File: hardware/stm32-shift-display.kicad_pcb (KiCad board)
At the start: 2 copper layers, 93.5 x 48.3 mm, 117 parts, among them J1 HDR_SWD, J2 USB_C_Receptacle_USB2.0_16P, SW1 SW_PUSH, SW2 SW_PUSH, SW3 SW_PUSH, SW4 SW_PUSH, SW5 218-2LPSTR, U1 AMS1117-3.3, U10 74HC595, U11 74HC595, U12 SM420561N, U13 SM420561N, U14 SM420561N, U2 STM32F103C8T6, U3 74HC595, U4 74HC595, U5 74HC595, U6 SM420561N, U7 SM420561N, U8 SM420561N, U9 74HC595, X1 OT32258MJBA4SL, X2 OK322532.768KJBA4SL

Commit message: Pre-autoroute on rev2
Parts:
- removed D4: BAT43, Diode_THT:D_DO-35_SOD27_P7.62mm_Horizontal
- removed G***: LOGO, CustomSymbols:GrackleLogo12mm
- removed JP1: SolderJumper_2_Open, Jumper:SolderJumper-2_P1.3mm_Open_RoundedPad1.0x1.5mm
- removed R10, R9: 10R, Resistor_SMD:R_0402_1005Metric
- removed R11: 10k, Resistor_SMD:R_0402_1005Metric
- removed R14, R15, R16, R17, R18, R19, R20, R21, R22, R23, R24, R25, R26, R27, R28, R29, R30, R31, R32, R33, R34, R35, R36, R37, R38, R39, R40, R41, R42, R43, R44, R45, R46, R47, R48, R49, R50, R51, R52, R53, R54, R55, R56, R57, R58, R59, R60: 470R, Resistor_SMD:R_0603_1608Metric
- removed R61: 22R, Resistor_THT:R_Axial_DIN0207_L6.3mm_D2.5mm_P7.62mm_Horizontal
- removed X2: OK322532.768KJBA4SL, Crystal:Crystal_SMD_3225-4Pin_3.2x2.5mm
- added BT1: 1060TR, Battery:BatteryHolder_Keystone_1060_1x2032, F.Cu at (144.8, 91.4)
- added C19: 100n, Capacitor_SMD:C_0402_1005Metric, B.Cu at (164.5, 78.5)
- added J3: HDR_UART, Connector_PinHeader_2.54mm:PinHeader_1x05_P2.54mm_Vertical, F.Cu at (194.7, 91.3)
- added RN1: 220R, Resistor_SMD:R_Array_Convex_4x0603, B.Cu at (139.7, 71.1)
- added RN10: 220R, Resistor_SMD:R_Array_Convex_4x0603, B.Cu at (190.4, 71.1)
- added RN11: 220R, Resistor_SMD:R_Array_Convex_4x0603, B.Cu at (180.2, 66.8)
- added RN12: 220R, Resistor_SMD:R_Array_Convex_4x0603, B.Cu at (190.4, 66.8)
- added RN13: 220R, Resistor_SMD:R_Array_Convex_4x0603, B.Cu at (126.6, 75.2)
- added RN2: 220R, Resistor_SMD:R_Array_Convex_4x0603, B.Cu at (149.7, 71.1)
- added RN3: 220R, Resistor_SMD:R_Array_Convex_4x0603, B.Cu at (139.7, 66.5)
- added RN4: 220R, Resistor_SMD:R_Array_Convex_4x0603, B.Cu at (149.7, 66.8)
- added RN5: 220R, Resistor_SMD:R_Array_Convex_4x0603, B.Cu at (159.9, 71.1)
- added RN6: 220R, Resistor_SMD:R_Array_Convex_4x0603, B.Cu at (170.1, 71.1)
- added RN7: 220R, Resistor_SMD:R_Array_Convex_4x0603, B.Cu at (159.9, 66.8)
- added RN8: 220R, Resistor_SMD:R_Array_Convex_4x0603, B.Cu at (170.1, 66.8)
- added RN9: 220R, Resistor_SMD:R_Array_Convex_4x0603, B.Cu at (180.2, 71.1)
- added U15: 74HC595, Package_SO:SOIC-16_3.9x9.9mm_P1.27mm, B.Cu at (166.9, 84.3)
- added Y1: Q13FC13500002, Crystal:Crystal_SMD_3215-2Pin_3.2x1.5mm, B.Cu at (174.1, 86.3)
- C1, C14, C15, C16, C17, C2, C6, C7, C8, R1, R12, SW5, U10, U11, U2, X1: moved to B.Cu
- C10, C9: value 100n -> 6p; moved to B.Cu
- C11, C12: footprint Capacitor_SMD:C_0402_1005Metric -> Capacitor_SMD:C_0805_2012Metric; moved to B.Cu
- C13: value 100n -> 10u; footprint Capacitor_SMD:C_0402_1005Metric -> Capacitor_Tantalum_SMD:CP_EIA-3216-18_Kemet-A; moved to B.Cu
- C18: value SCMR22C155PRBA0 -> 100n; footprint Mouser:SCMR22C155PRBA0 -> Capacitor_SMD:C_0402_1005Metric; moved to B.Cu
- C3, C4: footprint Capacitor_SMD:C_0805_2012Metric -> Capacitor_SMD:C_0402_1005Metric; moved to B.Cu
- C5: value 10u -> 100n; footprint Capacitor_Tantalum_SMD:CP_EIA-3216-18_Kemet-A -> Capacitor_SMD:C_0402_1005Metric; moved to B.Cu
- D1, D2, D3: value KT-0805Y -> LED_YLW; footprint LED_SMD:LED_0805_2012Metric -> LED_THT:LED_D3.0mm
- H1, H2, H3, H4: footprint MountingHole:MountingHole_3.2mm_M3_Pad_Via -> MountingHole:MountingHole_3.2mm_M3_ISO7380
- J1: value HDR_SWD -> GT-USB-7010ASV; footprint Connector_PinHeader_2.54mm:PinHeader_1x04_P2.54mm_Vertical -> easyeda2kicad:USB-C-SMD_G-SWITCH_GT-USB-7010ASV; moved to B.Cu
- J2: value USB_C_Receptacle_USB2.0_16P -> HDR_SWD; footprint Connector_USB:USB_C_Receptacle_HCTL_HC-TYPE-C-16P-01A -> Connector_PinHeader_2.54mm:PinHeader_1x04_P2.54mm_Vertical
- R13: value 470R -> 10k; footprint Resistor_SMD:R_0603_1608Metric -> Resistor_SMD:R_0402_1005Metric; moved to B.Cu
- R2, R3: value 10k -> 5k1; moved to B.Cu
- R4, R5: value 220R -> 0R; footprint Resistor_SMD:R_0603_1608Metric -> Resistor_SMD:R_0402_1005Metric; moved to B.Cu
- R6: value 220R -> 1k5; footprint Resistor_SMD:R_0603_1608Metric -> Resistor_SMD:R_0402_1005Metric; moved to B.Cu
- R7, R8: value 5k1 -> 10k; moved to B.Cu
- SW1: value SW_PUSH -> TS-1101-C-W; footprint Button_Switch_THT:SW_PUSH_6mm -> easyeda2kicad:SW-SMD_L6.0-W3.3-LS8.0; moved to B.Cu
- SW2, SW3, SW4: footprint Button_Switch_THT:SW_PUSH_6mm -> Mouser:TS046643BK160SMT
- U1: value AMS1117-3.3 -> USBLC6-2P6; footprint Package_TO_SOT_SMD:SOT-223-3_TabPin2 -> Package_TO_SOT_SMD:SOT-666; moved to B.Cu
- U12, U13, U8: value SM420561N -> VDMY10C0; footprint Display_7Segment:7SegmentLED_LTS6760_LTS6780 -> Mouser:VDMx10x0
- U14, U6, U7: value SM420561N -> 74HC595; footprint Display_7Segment:7SegmentLED_LTS6760_LTS6780 -> Package_SO:SOIC-16_3.9x9.9mm_P1.27mm; moved to B.Cu
- U3: value 74HC595 -> AMS1117-3.3; footprint Package_SO:SOIC-16_3.9x9.9mm_P1.27mm -> Package_TO_SOT_SMD:SOT-223-3_TabPin2; moved to B.Cu
- U4, U5, U9: value 74HC595 -> VDMY10C0; footprint Package_SO:SOIC-16_3.9x9.9mm_P1.27mm -> Mouser:VDMx10x0
- moved H4 82.3 mm to (203.2, 99.1)
- moved H3 79.8 mm to (127.0, 99.1)
- moved R6 70.6 mm to (191.3, 86.4), turned to 90 degrees
- moved R5 69.9 mm to (190.8, 84.8)
- moved R4 69.9 mm to (190.8, 83.8)
- moved U3 69.1 mm to (200.2, 70.9)
- moved R12 68.1 mm to (138.0, 93.1), turned to -90 degrees
- moved TP1 62.8 mm to (177.3, 55.9), turned to 90 degrees
- moved C12 62.2 mm to (199.1, 65.3), turned to 180 degrees
- moved TP2 61.8 mm to (180.9, 55.9), turned to 90 degrees
- moved TP3 60.9 mm to (184.4, 55.9), turned to 90 degrees
- moved TP4 59.9 mm to (188.0, 55.9), turned to 90 degrees
- moved TP5 59.1 mm to (191.5, 55.9), turned to 90 degrees
- moved C17 52.8 mm to (148.7, 78.5), turned to 180 degrees
- moved C13 49.1 mm to (198.9, 76.7), turned to 180 degrees
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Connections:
- C1 pad 1: VCC -> VBAT
- C10 pad 1: VCC -> GND
- C10 pad 2: GND -> /OSC32_OUT
- C11 pad 1: VCC -> VBUS
- C18 pad 1: Net-(C18-Pad1) -> VCC
- C2 pad 1: VBAT -> VCC
- C3 pad 1: VBUS -> VCC
- C7 pad 1: VBAT -> VCC
- C8 pad 1: VCC -> VBUS
- C9 pad 1: VCC -> GND
- C9 pad 2: GND -> /OSC32_IN
- J1 pad 1: VCC -> GND
- J1 pad 2: /SWDIO -> GND
- J1 pad 3: /SWCLK -> GND
- R12 pad 2: /Shift Display/~{SRCLR} -> /Shift Display/~{OE}
- R13 pad 1: /Shift Display/Q1A -> VCC
- R13 pad 2: /Shift Display/D1B -> /Shift Display/~{SRCLR}
- R2 pad 2: /BOOT0 -> /CC1
- R3 pad 2: /BOOT1 -> /CC2
- R4 pad 1: /LED1r -> /MCU_D-
- R4 pad 2: /LED1 -> /ESD_D-
- R5 pad 1: /LED2r -> /MCU_D+
- R5 pad 2: /LED2 -> /ESD_D+
- R6 pad 1: /LED3r -> VCC
- R6 pad 2: /LED3 -> /ESD_D+
- R7 pad 2: /CC1 -> /BOOT0
- R8 pad 2: /CC2 -> /BOOT1
- SW1 pad 2: /BTN1 -> /NRST
- SW2 pad 2: /BTN2 -> /BTN1
- SW3 pad 2: /BTN3 -> /BTN2
- SW4 pad 2: /NRST -> /BTN3
- U1 pad 1: GND -> /USB_D-
- U1 pad 2: VCC -> GND
- U1 pad 3: VBUS -> /USB_D+
- U10 pad 1: /Shift Display/Q4B -> /Shift Display/Q3B
- U10 pad 14: /Shift Display/SER3 -> /Shift Display/SER2
- U10 pad 15: /Shift Display/Q4A -> /Shift Display/Q3A
- U10 pad 2: /Shift Display/Q4C -> /Shift Display/Q3C
- U10 pad 3: /Shift Display/Q4D -> /Shift Display/Q3D
- U10 pad 4: /Shift Display/Q4E -> /Shift Display/Q3E
- U10 pad 5: /Shift Display/Q4F -> /Shift Display/Q3F
- U10 pad 6: /Shift Display/Q4G -> /Shift Display/Q3G
- U10 pad 7: /Shift Display/Q4H -> /Shift Display/Q3H
- U10 pad 9: /Shift Display/SER4 -> /Shift Display/SER3
- U11 pad 1: /Shift Display/Q6B -> /Shift Display/Q4B
- U11 pad 14: /Shift Display/SER5 -> /Shift Display/SER3
- U11 pad 15: /Shift Display/Q6A -> /Shift Display/Q4A
- U11 pad 2: /Shift Display/Q6C -> /Shift Display/Q4C
- U11 pad 3: /Shift Display/Q6D -> /Shift Display/Q4D
- U11 pad 4: /Shift Display/Q6E -> /Shift Display/Q4E
- U11 pad 5: /Shift Display/Q6F -> /Shift Display/Q4F
- U11 pad 6: /Shift Display/Q6G -> /Shift Display/Q4G
- U11 pad 7: /Shift Display/Q6H -> /Shift Display/Q4H
- U11 pad 9: unconnected-(U11-QH'-Pad9) -> /Shift Display/SER4
- U12 pad 1: /Shift Display/D2E -> /Shift Display/D5E
- U12 pad 10: /Shift Display/D2G -> /Shift Display/D5G
- U12 pad 2: /Shift Display/D2D -> /Shift Display/D5D
- U12 pad 4: /Shift Display/D2C -> /Shift Display/D5C
- U12 pad 5: /Shift Display/D2P -> /Shift Display/D5P
- U12 pad 6: /Shift Display/D2B -> /Shift Display/D5B
- U12 pad 7: /Shift Display/D2A -> /Shift Display/D5A
- U12 pad 9: /Shift Display/D2F -> /Shift Display/D5F
- U13 pad 1: /Shift Display/D4E -> /Shift Display/D6E
- U13 pad 10: /Shift Display/D4G -> /Shift Display/D6G
- U13 pad 2: /Shift Display/D4D -> /Shift Display/D6D
- U13 pad 4: /Shift Display/D4C -> /Shift Display/D6C
- U13 pad 5: /Shift Display/D4P -> /Shift Display/D6P
- U13 pad 6: /Shift Display/D4B -> /Shift Display/D6B
- U13 pad 7: /Shift Display/D4A -> /Shift Display/D6A
- U13 pad 9: /Shift Display/D4F -> /Shift Display/D6F
- U14 pad 1: /Shift Display/D6E -> /Shift Display/Q5B
- U14 pad 10: /Shift Display/D6G -> /Shift Display/~{SRCLR}
- U14 pad 2: /Shift Display/D6D -> /Shift Display/Q5C
- U14 pad 3: GND -> /Shift Display/Q5D
- U14 pad 4: /Shift Display/D6C -> /Shift Display/Q5E
- U14 pad 5: /Shift Display/D6P -> /Shift Display/Q5F
- U14 pad 6: /Shift Display/D6B -> /Shift Display/Q5G
- U14 pad 7: /Shift Display/D6A -> /Shift Display/Q5H
- U14 pad 9: /Shift Display/D6F -> /Shift Display/SER5
- U2 pad 10: /LED3 -> /Shift Display/~{OE}
- U2 pad 11: /LED2 -> /Shift Display/~{SRCLR}
- U2 pad 12: /LED1 -> /Shift Display/RCLK
- U2 pad 13: /BTN1 -> /Shift Display/SER
- U2 pad 14: /BTN2 -> /Shift Display/SRCLK
- U2 pad 15: /BTN3 -> unconnected-(U2-PA5-Pad15)
- U2 pad 21: unconnected-(U2-PB10-Pad21) -> /TX3
- U2 pad 22: unconnected-(U2-PB11-Pad22) -> /RX3
- U2 pad 26: unconnected-(U2-PB13-Pad26) -> /CTS3
- U2 pad 27: unconnected-(U2-PB14-Pad27) -> /RTS3
- U2 pad 39: /Shift Display/SER -> /BTN1
- U2 pad 4: unconnected-(U2-PC15-Pad4) -> /OSC32_OUT
- U2 pad 40: /Shift Display/SRCLK -> /BTN2
- U2 pad 41: /Shift Display/~{SRCLR} -> /BTN3
- U2 pad 42: /Shift Display/RCLK -> /LED1
- U2 pad 43: /Shift Display/~{OE} -> /LED2
- U2 pad 45: unconnected-(U2-PB8-Pad45) -> /LED3
- U3 pad 1: /Shift Display/Q1B -> GND
- U3 pad 2: /Shift Display/Q1C -> VCC
- U3 pad 3: /Shift Display/Q1D -> VBUS
- U4 pad 1: /Shift Display/Q3B -> /Shift Display/D1E
- U4 pad 10: /Shift Display/~{SRCLR} -> /Shift Display/D1G
- U4 pad 2: /Shift Display/Q3C -> /Shift Display/D1D
- U4 pad 3: /Shift Display/Q3D -> GND
- U4 pad 4: /Shift Display/Q3E -> /Shift Display/D1C
- U4 pad 5: /Shift Display/Q3F -> /Shift Display/D1P
- U4 pad 6: /Shift Display/Q3G -> /Shift Display/D1B
- U4 pad 7: /Shift Display/Q3H -> /Shift Display/D1A
- U4 pad 9: /Shift Display/SER3 -> /Shift Display/D1F
- U5 pad 1: /Shift Display/Q5B -> /Shift Display/D2E
- U5 pad 10: /Shift Display/~{SRCLR} -> /Shift Display/D2G
- U5 pad 2: /Shift Display/Q5C -> /Shift Display/D2D
- U5 pad 3: /Shift Display/Q5D -> GND
- U5 pad 4: /Shift Display/Q5E -> /Shift Display/D2C
- U5 pad 5: /Shift Display/Q5F -> /Shift Display/D2P
- U5 pad 6: /Shift Display/Q5G -> /Shift Display/D2B
- U5 pad 7: /Shift Display/Q5H -> /Shift Display/D2A
- U5 pad 9: /Shift Display/SER5 -> /Shift Display/D2F
- U6 pad 1: /Shift Display/D1E -> /Shift Display/Q1B
- U6 pad 10: /Shift Display/D1G -> /Shift Display/~{SRCLR}
- U6 pad 2: /Shift Display/D1D -> /Shift Display/Q1C
- U6 pad 3: GND -> /Shift Display/Q1D
- U6 pad 4: /Shift Display/D1C -> /Shift Display/Q1E
- U6 pad 5: /Shift Display/D1P -> /Shift Display/Q1F
- U6 pad 6: /Shift Display/D1B -> /Shift Display/Q1G
- U6 pad 7: /Shift Display/D1A -> /Shift Display/Q1H
- U6 pad 9: /Shift Display/D1F -> /Shift Display/SER1
- U7 pad 1: /Shift Display/D3E -> /Shift Display/Q2B
- U7 pad 10: /Shift Display/D3G -> /Shift Display/~{SRCLR}
- U7 pad 2: /Shift Display/D3D -> /Shift Display/Q2C
- U7 pad 3: GND -> /Shift Display/Q2D
- U7 pad 4: /Shift Display/D3C -> /Shift Display/Q2E
- U7 pad 5: /Shift Display/D3P -> /Shift Display/Q2F
- U7 pad 6: /Shift Display/D3B -> /Shift Display/Q2G
- U7 pad 7: /Shift Display/D3A -> /Shift Display/Q2H
- U7 pad 9: /Shift Display/D3F -> /Shift Display/SER2
- U8 pad 1: /Shift Display/D5E -> /Shift Display/D3E
- U8 pad 10: /Shift Display/D5G -> /Shift Display/D3G
- U8 pad 2: /Shift Display/D5D -> /Shift Display/D3D
- U8 pad 4: /Shift Display/D5C -> /Shift Display/D3C
- U8 pad 5: /Shift Display/D5P -> /Shift Display/D3P
- U8 pad 6: /Shift Display/D5B -> /Shift Display/D3B
- U8 pad 7: /Shift Display/D5A -> /Shift Display/D3A
- U8 pad 9: /Shift Display/D5F -> /Shift Display/D3F
- U9 pad 1: /Shift Display/Q2B -> /Shift Display/D4E
- U9 pad 10: /Shift Display/~{SRCLR} -> /Shift Display/D4G
- U9 pad 2: /Shift Display/Q2C -> /Shift Display/D4D
- U9 pad 3: /Shift Display/Q2D -> GND
- U9 pad 4: /Shift Display/Q2E -> /Shift Display/D4C
- U9 pad 5: /Shift Display/Q2F -> /Shift Display/D4P
- U9 pad 6: /Shift Display/Q2G -> /Shift Display/D4B
- U9 pad 7: /Shift Display/Q2H -> /Shift Display/D4A
- U9 pad 9: /Shift Display/SER2 -> /Shift Display/D4F
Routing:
- net VCC: track 244.8 -> 46.8 mm, vias 8 -> 9
- net /Shift Display/~{SRCLR}: track 155.0 -> 0.00 mm, vias 10 -> 0
- net /Shift Display/~{OE}: track 149.5 -> 0.00 mm, vias 11 -> 0
- net /Shift Display/SRCLK: track 142.7 -> 0.00 mm, vias 10 -> 0
- net /Shift Display/RCLK: track 142.3 -> 0.00 mm, vias 8 -> 0
- net /Shift Display/SER: track 104.9 -> 0.00 mm, vias 8 -> 0
- net GND: track 94.6 -> 25.5 mm, vias 37 -> 15
- net /LED3: track 62.7 -> 0.00 mm
- net /LED2: track 62.1 -> 0.00 mm
- net /LED1: track 61.6 -> 0.00 mm
- net VBAT: track 39.4 -> 2.55 mm, vias 2 -> 0
- net /Shift Display/SER2: track 32.1 -> 0.00 mm, vias 2 -> 0
- net /Shift Display/SER4: track 30.9 -> 0.00 mm, vias 2 -> 0
- net /SWCLK: track 28.0 -> 0.00 mm
- net /SWDIO: track 27.8 -> 0.00 mm
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- added copper zone on In1.Cu, net GND
- added copper zone on B.Cu, net VCC
- added copper zone on In2.Cu, net VCC
- removed copper zone on F.Cu, net VCC
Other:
- board size 93.5 x 48.3 mm -> 83.8 x 49.5 mm
- copper layers 2 -> 4
- board text removed: "+"
- board text removed: "-"
- board text removed: "0"
- board text removed: "1"
- board text removed: "3V3"
- board text removed: "A"
- board text removed: "B"
- board text removed: "BOOT"
- board text removed: "C"
- board text removed: "CC"
- board text removed: "CLK"
- board text removed: "D"
- board text removed: "DIO"
- board text removed: "DP"
- board text removed: "E"
- board text removed: "F"
- board text removed: "G"
- board text removed: "GND"
- board text removed: "JLCJLCJLC"
- board text removed: "NRST"
- board text removed: "RCLK"
- board text removed: "SER"
- board text removed: "SET"
- board text removed: "SRCLK"
- board text removed: "STM32 Shift Display"
- board text removed: "rev 0"
- board text removed: "~{OE}"
- board text removed: "~{SRCLR}"

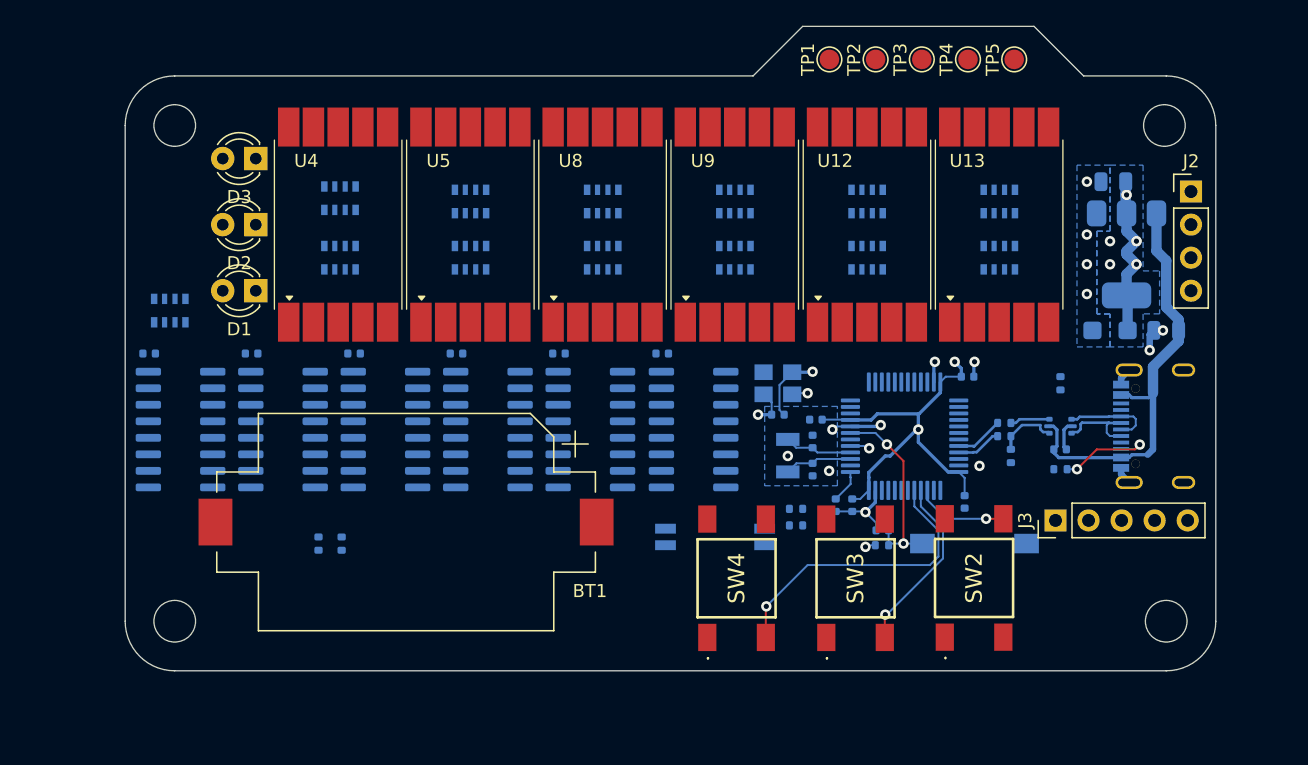
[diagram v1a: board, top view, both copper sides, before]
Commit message: Initial rev2 design, layout, routing, and mech done. Order submitted.
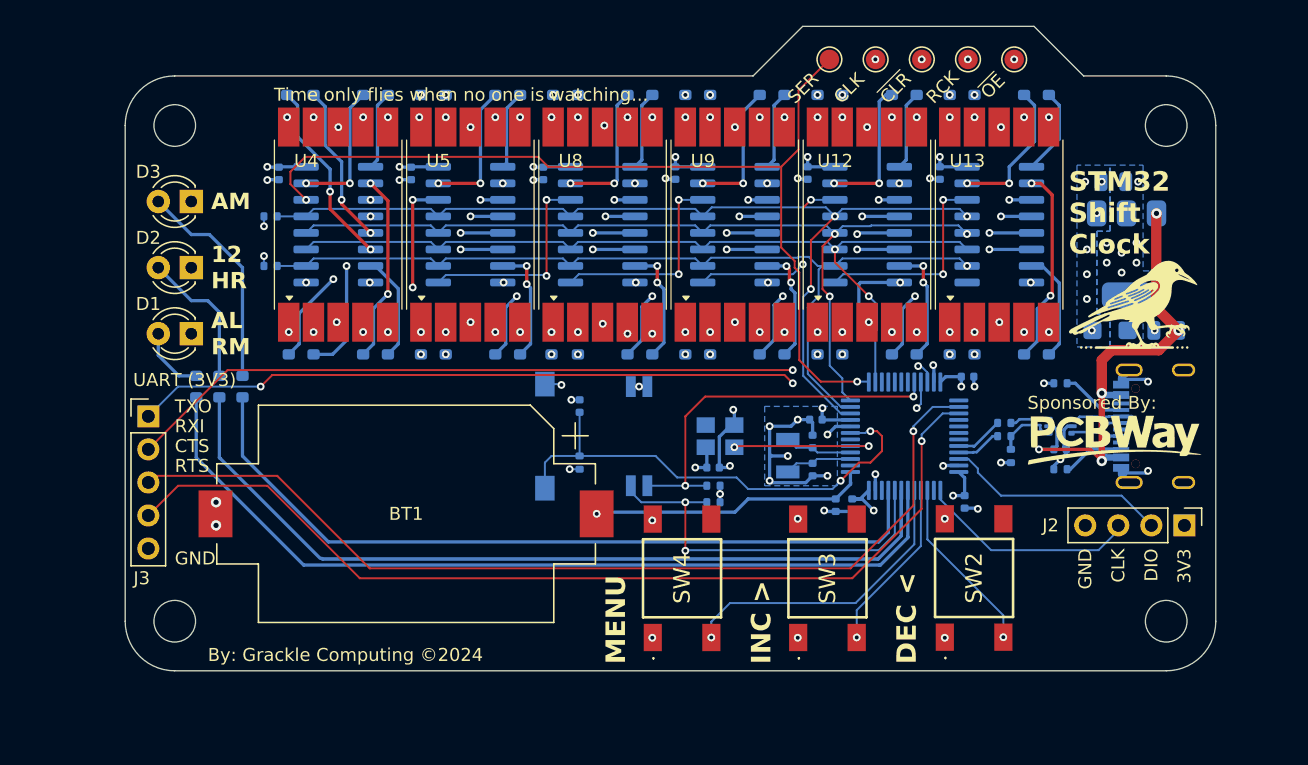
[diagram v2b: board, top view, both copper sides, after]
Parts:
- removed RN1, RN10, RN11, RN12, RN13, RN2, RN3, RN4, RN5, RN6, RN7, RN8, RN9: 220R, Resistor_SMD:R_Array_Convex_4x0603
- added G***: LOGO, CustomSymbols:PCBWayLogo15x4mm, F.Cu at (200.0, 85.0)
- added G***: LOGO, CustomSymbols:GrackleLogo12mm, F.Cu at (200.9, 74.7)
- added R10: 220R, Resistor_SMD:R_0603_1608Metric, B.Cu at (143.4, 59.4)
- added R11: 220R, Resistor_SMD:R_0603_1608Metric, B.Cu at (141.5, 77.7)
- added R14: 220R, Resistor_SMD:R_0603_1608Metric, B.Cu at (137.7, 77.7)
- added R15: 220R, Resistor_SMD:R_0603_1608Metric, B.Cu at (135.8, 77.7)
- added R16: 220R, Resistor_SMD:R_0603_1608Metric, B.Cu at (137.7, 59.4)
- added R17: 220R, Resistor_SMD:R_0603_1608Metric, B.Cu at (135.6, 59.4)
- added R18: 220R, Resistor_SMD:R_0603_1608Metric, B.Cu at (143.4, 77.7)
- added R19: 220R, Resistor_SMD:R_0603_1608Metric, B.Cu at (151.6, 59.4)
- added R20: 220R, Resistor_SMD:R_0603_1608Metric, B.Cu at (153.5, 59.4)
- added R21: 220R, Resistor_SMD:R_0603_1608Metric, B.Cu at (151.6, 77.7)
- added R22: 220R, Resistor_SMD:R_0603_1608Metric, B.Cu at (147.8, 77.7)
- added R23: 220R, Resistor_SMD:R_0603_1608Metric, B.Cu at (145.9, 77.7)
- added R24: 220R, Resistor_SMD:R_0603_1608Metric, B.Cu at (147.8, 59.4)
- added R25: 220R, Resistor_SMD:R_0603_1608Metric, B.Cu at (145.9, 59.4)
- added R26: 220R, Resistor_SMD:R_0603_1608Metric, B.Cu at (153.5, 77.7)
- added R27: 220R, Resistor_SMD:R_0603_1608Metric, B.Cu at (161.8, 59.4)
- added R28: 220R, Resistor_SMD:R_0603_1608Metric, B.Cu at (163.7, 59.4)
- added R29: 220R, Resistor_SMD:R_0603_1608Metric, B.Cu at (161.8, 77.7)
- added R30: 220R, Resistor_SMD:R_0603_1608Metric, B.Cu at (158.0, 77.7)
- added R31: 220R, Resistor_SMD:R_0603_1608Metric, B.Cu at (156.0, 77.7)
- added R32: 220R, Resistor_SMD:R_0603_1608Metric, B.Cu at (158.0, 59.4)
- added R33: 220R, Resistor_SMD:R_0603_1608Metric, B.Cu at (156.1, 59.4)
- added R34: 220R, Resistor_SMD:R_0603_1608Metric, B.Cu at (163.7, 77.7)
- added R35: 220R, Resistor_SMD:R_0603_1608Metric, B.Cu at (172.0, 59.4)
- added R36: 220R, Resistor_SMD:R_0603_1608Metric, B.Cu at (173.9, 59.4)
- added R37: 220R, Resistor_SMD:R_0603_1608Metric, B.Cu at (172.0, 77.7)
- added R38: 220R, Resistor_SMD:R_0603_1608Metric, B.Cu at (168.1, 77.7)
- added R39: 220R, Resistor_SMD:R_0603_1608Metric, B.Cu at (166.2, 77.7)
- added R40: 220R, Resistor_SMD:R_0603_1608Metric, B.Cu at (168.1, 59.4)
- added R41: 220R, Resistor_SMD:R_0603_1608Metric, B.Cu at (166.2, 59.4)
- added R42: 220R, Resistor_SMD:R_0603_1608Metric, B.Cu at (173.9, 77.7)
- added R43: 220R, Resistor_SMD:R_0603_1608Metric, B.Cu at (182.1, 59.4)
- added R44: 220R, Resistor_SMD:R_0603_1608Metric, B.Cu at (184.0, 59.4)
- added R45: 220R, Resistor_SMD:R_0603_1608Metric, B.Cu at (182.1, 77.7)
- added R46: 220R, Resistor_SMD:R_0603_1608Metric, B.Cu at (178.3, 77.7)
- added R47: 220R, Resistor_SMD:R_0603_1608Metric, B.Cu at (176.4, 77.7)
- added R48: 220R, Resistor_SMD:R_0603_1608Metric, B.Cu at (178.3, 59.4)
- added R49: 220R, Resistor_SMD:R_0603_1608Metric, B.Cu at (176.4, 59.4)
- added R50: 220R, Resistor_SMD:R_0603_1608Metric, B.Cu at (184.0, 77.7)
- added R51: 220R, Resistor_SMD:R_0603_1608Metric, B.Cu at (192.3, 59.4)
- added R52: 220R, Resistor_SMD:R_0603_1608Metric, B.Cu at (194.2, 59.4)
- added R53: 220R, Resistor_SMD:R_0603_1608Metric, B.Cu at (192.3, 77.7)
- added R54: 220R, Resistor_SMD:R_0603_1608Metric, B.Cu at (188.5, 77.7)
- added R55: 220R, Resistor_SMD:R_0603_1608Metric, B.Cu at (186.6, 77.7)
- added R56: 220R, Resistor_SMD:R_0603_1608Metric, B.Cu at (188.5, 59.4)
- added R57: 220R, Resistor_SMD:R_0603_1608Metric, B.Cu at (186.6, 59.4)
- added R58: 220R, Resistor_SMD:R_0603_1608Metric, B.Cu at (194.2, 77.7)
- added R59: 220R, Resistor_SMD:R_0603_1608Metric, B.Cu at (128.7, 81.0)
- added R60: 220R, Resistor_SMD:R_0603_1608Metric, B.Cu at (130.4, 81.0)
- added R61: 220R, Resistor_SMD:R_0603_1608Metric, B.Cu at (132.2, 81.0)
- added R9: 220R, Resistor_SMD:R_0603_1608Metric, B.Cu at (141.5, 59.4)
- added REF**: KiCad-Logo2_5mm_SilkScreen, Symbol:KiCad-Logo2_5mm_SilkScreen, B.Cu at (144.8, 90.2)
- moved J3 70.2 mm to (125.0, 83.3), turned to 0 degrees
- moved SW1 34.0 mm to (155.4, 84.8), turned to -90 degrees
- moved C17 30.3 mm to (175.6, 64.6), turned to -90 degrees
- moved U15 28.3 mm to (190.4, 68.6)
- moved U14 26.5 mm to (180.2, 68.6)
- moved J2 25.7 mm to (204.6, 91.7), turned to -90 degrees
- moved C19 25.4 mm to (185.8, 64.6), turned to -90 degrees
- moved R12 25.4 mm to (134.4, 67.9), turned to 0 degrees
- moved C6 25.2 mm to (158.1, 82.5), turned to -90 degrees
- moved U11 24.7 mm to (170.1, 68.6)
- moved R1 24.1 mm to (158.1, 86.9), turned to -90 degrees
- moved U10 23.0 mm to (159.9, 68.6)
- moved R13 22.0 mm to (134.4, 71.8), turned to 0 degrees
- moved U7 21.3 mm to (149.7, 68.6)
- moved C16 20.1 mm to (155.3, 64.6), turned to -90 degrees
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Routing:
- net /LED2: track 0.00 -> 113.4 mm
- net /Shift Display/~{SRCLR}: track 0.00 -> 87.4 mm, vias 0 -> 2
- net /Shift Display/~{OE}: track 0.00 -> 87.2 mm, vias 0 -> 4
- net /Shift Display/SRCLK: track 0.00 -> 83.2 mm, vias 0 -> 3
- net /Shift Display/RCLK: track 0.00 -> 81.6 mm, vias 0 -> 4
- net /RTS3: track 0.00 -> 74.8 mm, vias 0 -> 1
- net /CTS3: track 0.00 -> 74.2 mm, vias 0 -> 1
- net /Shift Display/SER: track 0.00 -> 72.4 mm, vias 0 -> 2
- net /LED1: track 0.00 -> 67.3 mm
- net /TX3: track 0.00 -> 63.6 mm, vias 0 -> 3
- net /RX3: track 0.00 -> 63.5 mm, vias 0 -> 2
- net /LED3: track 0.00 -> 60.4 mm
- net GND: track 25.5 -> 57.5 mm, vias 15 -> 61
- net /BOOT0: track 0.00 -> 29.9 mm, vias 0 -> 2
- net /BOOT1: track 0.00 -> 29.2 mm, vias 0 -> 2
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- added copper zone on In2.Cu, net GND
- added copper zone on In1.Cu, net VCC
- removed copper zone on In1.Cu, net GND
- removed copper zone on In2.Cu, net VCC
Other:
- board text added: "12 HR"
- board text added: "3V3"
- board text added: "AL RM"
- board text added: "AM"
- board text added: "BOOT0"
- board text added: "BOOT1"
- board text added: "By: Grackle Computing ©2024"
- board text added: "CLK"
- board text added: "CTS"
- board text added: "DEC <"
- board text added: "DIO"
- board text added: "GND"
- board text added: "INC >"
- board text added: "MENU"
- board text added: "NRST"
- board text added: "RCK"
- board text added: "RTS"
- board text added: "RXI"
- board text added: "Rev 1"
- board text added: "SER"
- board text added: "STM32 Shift Clock"
- board text added: "Sponsored By:"
- board text added: "TXO"
- board text added: "Time only flies when no one is watching..."
- board text added: "UART (3V3)"
- board text added: "WayWayWay"
- board text added: "~{CLR}"
- board text added: "~{OE}"
